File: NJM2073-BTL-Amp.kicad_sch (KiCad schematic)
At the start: 71 parts, among them J1 Screw_Terminal_01x02, J2 Screw_Terminal_01x02, U3 NJM4558, U4 NJM4558

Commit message: ラベル名変更
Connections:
- net Input renamed Input_L
- net Input_L: no longer C23.1
- new net Input_R: C23.1
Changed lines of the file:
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@@
 		)
 	)
-	(global_label "Input"
+	(global_label "Input_L"
 		(shape input)
 		(at 110.49 91.44 180)
@@
 		)
 		(property "Intersheetrefs" "${INTERSHEET_REFS}"
-			(at 102.7273 91.44 0)
+			(at 100.7316 91.44 0)
 			(effects
 				(font
@@
 		)
 	)
-	(global_label "Input"
+	(global_label "Input_R"
 		(shape input)
 		(at 110.49 180.34 180)
@@
 		)
 		(property "Intersheetrefs" "${INTERSHEET_REFS}"
-			(at 102.7273 180.34 0)
+			(at 100.4897 180.34 0)
 			(effects
 				(font

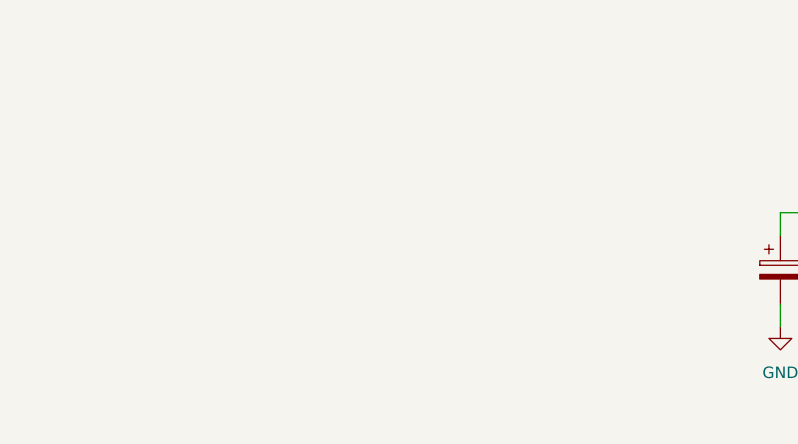
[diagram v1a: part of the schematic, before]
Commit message: 電源入力・フィルタ追加
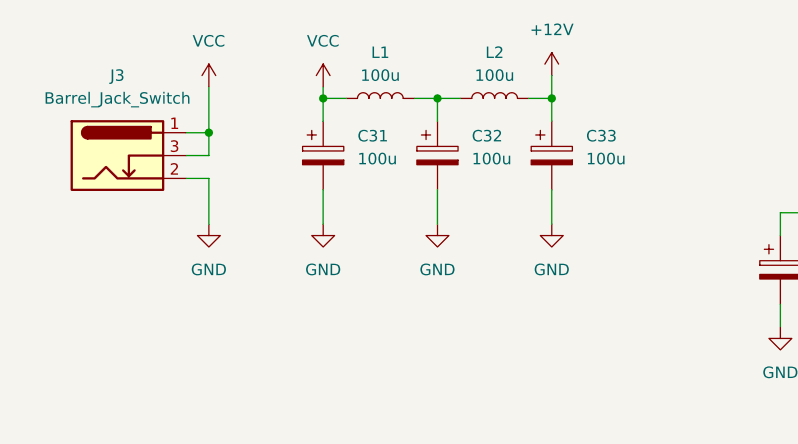
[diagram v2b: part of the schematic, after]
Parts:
- added C31, C32, C33: 100u, symbol Device:C_Polarized
- added J3: Barrel_Jack_Switch, symbol Connector:Barrel_Jack_Switch
- added L1, L2: 100u, symbol Device:L
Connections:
- net +12V: now also C33.1, L2.2
- net GND: now also C31.2, C32.2, C33.2, J3.2
- new net: C32.1, L1.2, L2.1
- new net VCC: C31.1, J3.1, J3.3, L1.1

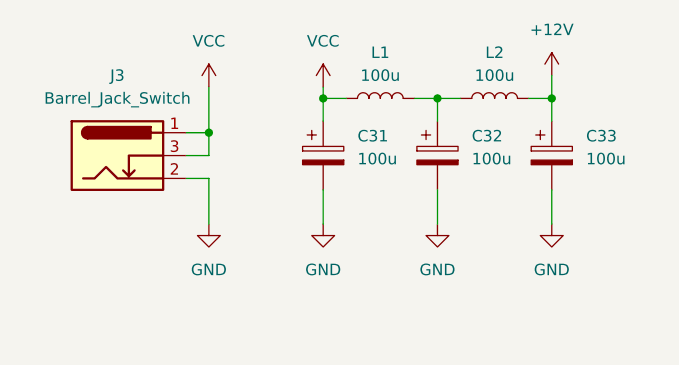
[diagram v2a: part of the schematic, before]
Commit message: 逆接保護ダイオード追加
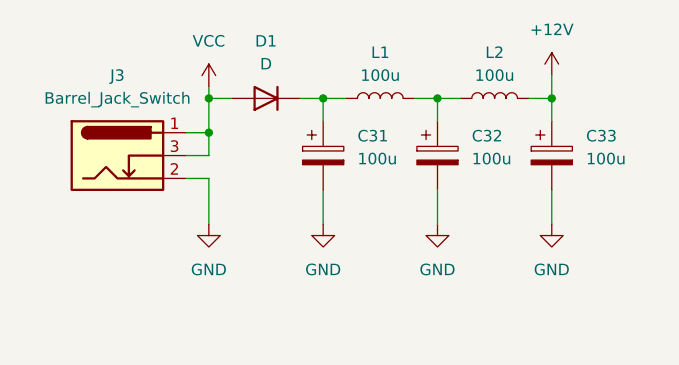
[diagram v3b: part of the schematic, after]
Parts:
- added D1: D, symbol Device:D
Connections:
- net VCC: now also D1.2 (A); no longer C31.1, L1.1
- new net: C31.1, D1.1 (K), L1.1
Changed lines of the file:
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@@
 	(paper "A3")
 	(junction
+		(at 50.8 25.4)
+		(diameter 0)
+		(color 0 0 0 0)
+	)
+	(junction
 		(at 114.3 127)
 		(diameter 0)
@@
 	)
 	(junction
+		(at 38.1 25.4)
+		(diameter 0)
+		(color 0 0 0 0)
+	)
+	(junction
 		(at 163.83 38.1)
 		(diameter 0)
@@
 	)
 	(junction
-		(at 50.8 25.4)
-		(diameter 0)
-		(color 0 0 0 0)
-	)
-	(junction
 		(at 139.7 73.66)
 		(diameter 0)
@@
 	(wire
 		(pts
+			(xy 48.26 25.4) (xy 50.8 25.4)
+		)
+		(stroke
+			(width 0)
+			(type default)
+		)
+	)
+	(wire
+		(pts
 			(xy 304.8 62.23) (xy 304.8 63.5)
 		)
@@
 	(wire
 		(pts
+			(xy 38.1 25.4) (xy 40.64 25.4)
+		)
+		(stroke
+			(width 0)
+			(type default)
+		)
+	)
+	(wire
+		(pts
 			(xy 203.2 176.53) (xy 203.2 177.8)
 		)
@@
 	(wire
 		(pts
-			(xy 38.1 24.13) (xy 38.1 29.21)
+			(xy 38.1 24.13) (xy 38.1 25.4)
 		)
 		(stroke
@@
 	(wire
 		(pts
-			(xy 50.8 24.13) (xy 50.8 25.4)
-		)
-		(stroke
-			(width 0)
-			(type default)
-		)
-	)
-	(wire
-		(pts
 			(xy 139.7 175.26) (xy 144.78 175.26)
 		)
@@
 	(wire
 		(pts
+			(xy 38.1 25.4) (xy 38.1 29.21)
+		)
+		(stroke
+			(width 0)
+			(type default)
+		)
+	)
+	(wire
+		(pts
 			(xy 163.83 125.73) (xy 163.83 127)
 		)
@@
 	)
 	(symbol
-		(lib_id "power:VCC")
-		(at 50.8 24.13 0)
-		(unit 1)
-		(exclude_from_sim no)
-		(in_bom yes)
-		(on_board yes)
-		(dnp no)
-		(fields_autoplaced yes)
-		(property "Reference" "#PWR035"
-			(at 50.8 27.94 0)
-			(effects
-				(font
-					(size 1.27 1.27)
-				)
-				(hide yes)
-			)
-		)
-		(property "Value" "VCC"
-			(at 50.8 19.05 0)
-			(effects
-				(font
-					(size 1.27 1.27)
-				)
-			)
-		)
-		(property "Footprint" ""
-			(at 50.8 24.13 0)
-			(effects
-				(font
-					(size 1.27 1.27)
-				)
-				(hide yes)
-			)
-		)
-		(property "Datasheet" ""
-			(at 50.8 24.13 0)
-			(effects
-				(font
-					(size 1.27 1.27)
-				)
-				(hide yes)
-			)
-		)
-		(property "Description" "Power symbol creates a global label with name \"VCC\""
-			(at 50.8 24.13 0)
-			(effects
-				(font
-					(size 1.27 1.27)
-				)
-				(hide yes)
-			)
-		)
-		(pin "1"
-		)
-		(instances
-			(project "NJM2073-BTL-Amp"
-				(path "/39400954-8ff9-4acb-a709-09671291994b"
-					(reference "#PWR035")
-					(unit 1)
-				)
-			)
-		)
-	)
-	(symbol
 		(lib_id "Device:R")
 		(at 335.28 165.1 90)
@@
 				)
 			)
+		)
+	)
+	(symbol
+		(lib_id "Device:D")
+		(at 44.45 25.4 180)
+		(unit 1)
+		(exclude_from_sim no)
+		(in_bom yes)
+		(on_board yes)
+		(dnp no)
+		(fields_autoplaced yes)
+		(property "Reference" "D1"
+			(at 44.45 19.05 0)
+			(effects
+				(font
+					(size 1.27 1.27)
+				)
+			)
+		)
+		(property "Value" "D"
+			(at 44.45 21.59 0)
+			(effects
+				(font
+					(size 1.27 1.27)
+				)
+			)
+		)
+		(property "Footprint" ""
+			(at 44.45 25.4 0)
+			(effects
+				(font
+					(size 1.27 1.27)
+				)
+				(hide yes)
+			)
+		)
+		(property "Datasheet" "~"
+			(at 44.45 25.4 0)
+			(effects
+				(font
+					(size 1.27 1.27)
+				)
+				(hide yes)
+			)
+		)
+		(property "Description" "Diode"
+			(at 44.45 25.4 0)
+			(effects
+				(font
+					(size 1.27 1.27)
+				)
+				(hide yes)
+			)
+		)
+		(property "Sim.Device" "D"
+			(at 44.45 25.4 0)
+			(effects
+				(font
+					(size 1.27 1.27)
+				)
+				(hide yes)
+			)
+		)
+		(property "Sim.Pins" "1=K 2=A"
+			(at 44.45 25.4 0)
+			(effects
+				(font
+					(size 1.27 1.27)
+				)
+				(hide yes)
+			)
+		)
+		(pin "2"
+		)
+		(pin "1"
+		)
+		(instances
+			(project ""
+				(path "/39400954-8ff9-4acb-a709-09671291994b"
+					(reference "D1")
+					(unit 1)
+				)
+			)

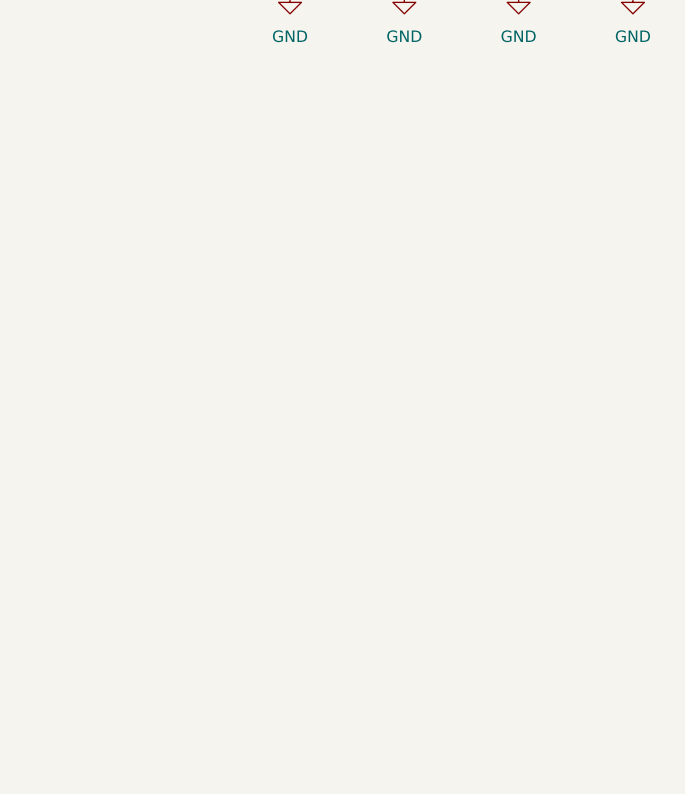
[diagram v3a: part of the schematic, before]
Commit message: 音声入力追加
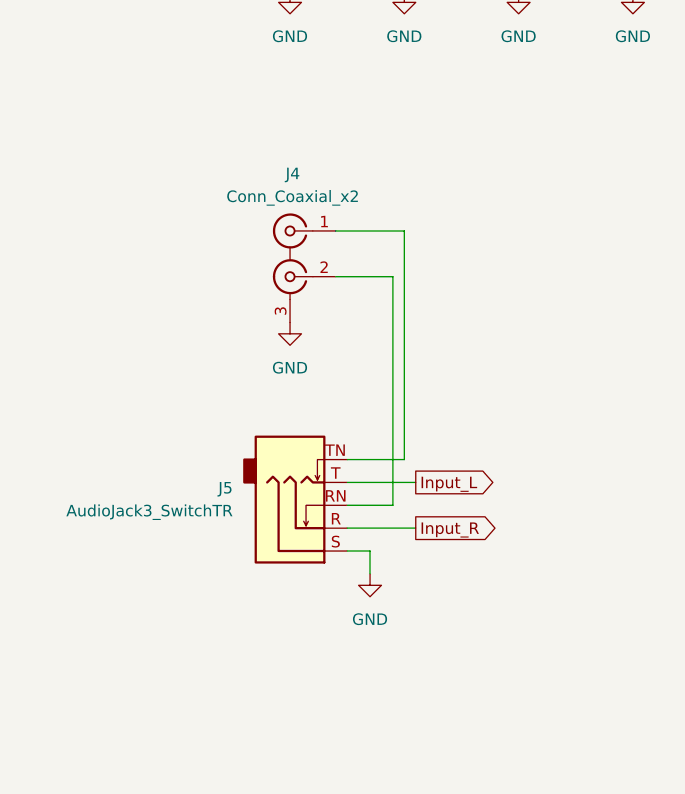
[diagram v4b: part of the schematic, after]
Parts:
- added J4: Conn_Coaxial_x2, symbol Connector:Conn_Coaxial_x2
- added J5: AudioJack3_SwitchTR, symbol Connector_Audio:AudioJack3_SwitchTR
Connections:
- net GND: now also J4.3 (EXT), J5.S
- net Input_L: now also J5.T
- net Input_R: now also J5.R
- new net: J4.2 (IN2), J5.RN
- new net: J4.1 (IN1), J5.TN

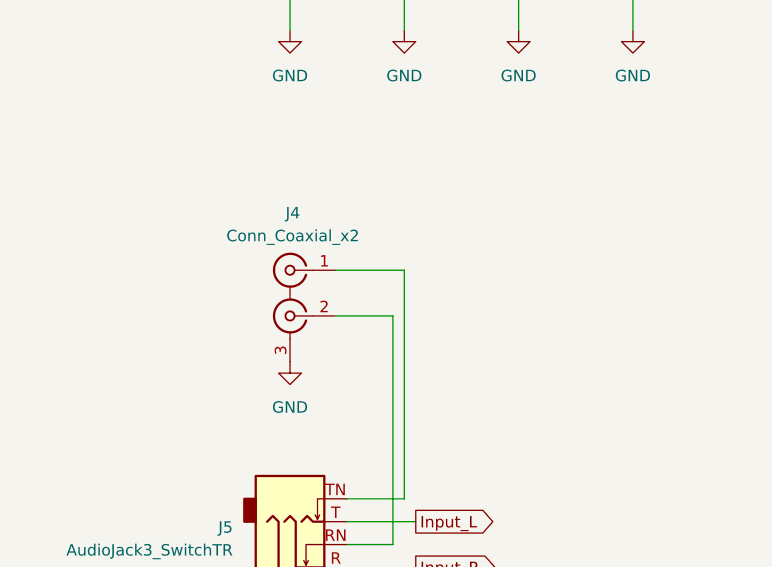
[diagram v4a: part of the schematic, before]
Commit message: フットプリント割り当て
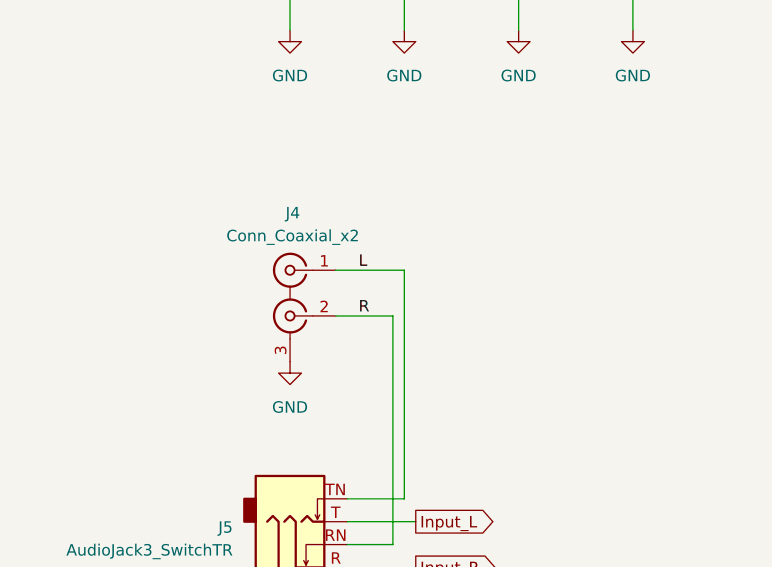
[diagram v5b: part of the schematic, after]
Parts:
- C1, C11, C12, C13, C14, C15, C16, C17, C18, C2, Copt1, Copt2: footprint (none) -> Capacitor_THT:C_Disc_D5.0mm_W2.5mm_P5.00mm
- C27, C28, C29, C30, C31, C32, C33, L1, L2: footprint (none) -> Capacitor_THT:CP_Radial_D10.0mm_P5.00mm
- D1: footprint (none) -> Diode_THT:D_A-405_P12.70mm_Horizontal
- J3: footprint (none) -> Connector_BarrelJack:BarrelJack_Horizontal
- J5: footprint (none) -> Connector_Audio:Jack_3.5mm_CUI_SJ1-3535NG_Horizontal
- RV1, RV2, RV3: footprint (none) -> Potentiometer_THT:Potentiometer_Alps_RK097_Dual_Horizontal
- Rf1, Rf2, Rf3, Rf4, Ropt1, Ropt2, Rs1, Rs2, Rs3, Rs4: footprint (none) -> Resistor_THT:R_Axial_DIN0207_L6.3mm_D2.5mm_P10.16mm_Horizontal
- U1, U2: footprint (none) -> Package_DIP:DIP-8_W7.62mm_Socket
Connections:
- net R: now reaches J4.2 (IN2), J5.RN
- net L: now reaches J4.1 (IN1), J5.TN
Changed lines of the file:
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@@
 		)
 	)
+	(label "R"
+		(at 45.72 71.12 0)
+		(fields_autoplaced yes)
+		(effects
+			(font
+				(size 1.27 1.27)
+			)
+			(justify left bottom)
+		)
+	)
+	(label "L"
+		(at 45.72 66.04 0)
+		(fields_autoplaced yes)
+		(effects
+			(font
+				(size 1.27 1.27)
+			)
+			(justify left bottom)
+		)
+	)
 	(global_label "Input_R"
 		(shape output)
@@
 			)
 		)
-		(property "Footprint" ""
+		(property "Footprint" "Potentiometer_THT:Potentiometer_Alps_RK097_Dual_Horizontal"
 			(at 203.2 50.8 0)
 			(effects
@@
 			)
 		)
-		(property "Footprint" ""
+		(property "Footprint" "Connector_Audio:Jack_3.5mm_CUI_SJ1-3535NG_Horizontal"
 			(at 39.37 99.06 0)
 			(effects
@@
 			)
 		)
-		(property "Footprint" ""
+		(property "Footprint" "Resistor_THT:R_Axial_DIN0207_L6.3mm_D2.5mm_P10.16mm_Horizontal"
 			(at 366.522 63.5 90)
 			(effects
@@
 			)
 		)
-		(property "Footprint" ""
+		(property "Footprint" "Package_DIP:DIP-8_W7.62mm_Socket"
 			(at 342.9 145.288 0)
 			(effects
@@
 			)
 		)
-		(property "Footprint" ""
+		(property "Footprint" "Capacitor_THT:C_Disc_D5.0mm_W2.5mm_P5.00mm"
 			(at 305.7652 151.13 0)
 			(effects
@@
 			)
 		)
-		(property "Footprint" ""
+		(property "Footprint" "Capacitor_THT:C_Disc_D5.0mm_W2.5mm_P5.00mm"
 			(at 324.8152 173.99 0)
 			(effects
@@
 			)
 		)
-		(property "Footprint" ""
+		(property "Footprint" "Capacitor_THT:C_Disc_D5.0mm_W2.5mm_P5.00mm"
 			(at 305.7652 99.06 0)
 			(effects
@@
 			)
 		)
-		(property "Footprint" ""
+		(property "Footprint" "Capacitor_THT:CP_Radial_D10.0mm_P5.00mm"
 			(at 102.5652 137.16 0)
 			(effects
@@
 			)
 		)
-		(property "Footprint" ""
+		(property "Footprint" "Resistor_THT:R_Axial_DIN0207_L6.3mm_D2.5mm_P10.16mm_Horizontal"
 			(at 317.5 65.278 90)
 			(effects
@@
 			)
 		)
-		(property "Footprint" ""
+		(property "Footprint" "Capacitor_THT:CP_Radial_D10.0mm_P5.00mm"
 			(at 64.4652 35.56 0)
 			(effects
@@
 			)
 		)
-		(property "Footprint" ""
+		(property "Footprint" "Resistor_THT:R_Axial_DIN0207_L6.3mm_D2.5mm_P10.16mm_Horizontal"
 			(at 317.5 154.178 90)
 			(effects
@@
 			)
 		)
-		(property "Footprint" ""
+		(property "Footprint" "Capacitor_THT:CP_Radial_D10.0mm_P5.00mm"
 			(at 77.1652 35.56 0)
 			(effects
@@
 			)
 		)
-		(property "Footprint" ""
+		(property "Footprint" "Resistor_THT:R_Axial_DIN0207_L6.3mm_D2.5mm_P10.16mm_Horizontal"
 			(at 335.28 65.278 90)
 			(effects
@@
 			)
 		)
-		(property "Footprint" ""
+		(property "Footprint" "Capacitor_THT:C_Disc_D5.0mm_W2.5mm_P5.00mm"
 			(at 305.7652 62.23 0)
 			(effects
@@
 			)
 		)
-		(property "Footprint" ""
+		(property "Footprint" "Resistor_THT:R_Axial_DIN0207_L6.3mm_D2.5mm_P10.16mm_Horizontal"
 			(at 317.5 77.978 90)
 			(effects
@@
 			)
 		)
-		(property "Footprint" ""
+		(property "Footprint" "Capacitor_THT:C_Disc_D5.0mm_W2.5mm_P5.00mm"
 			(at 356.5652 130.81 0)
 			(effects
@@
 			)
 		)
-		(property "Footprint" ""
+		(property "Footprint" "Package_DIP:DIP-8_W7.62mm_Socket"
 			(at 342.9 56.388 0)
 			(effects
@@
 			)
 		)
-		(property "Footprint" ""
+		(property "Footprint" "Resistor_THT:R_Axial_DIN0207_L6.3mm_D2.5mm_P10.16mm_Horizontal"
 			(at 335.28 77.978 90)
 			(effects
@@
 			)
 		)
-		(property "Footprint" ""
+		(property "Footprint" "Capacitor_THT:C_Disc_D5.0mm_W2.5mm_P5.00mm"
 			(at 324.8152 151.13 0)
 			(effects
@@
 			)
 		)
-		(property "Footprint" ""
+		(property "Footprint" "Capacitor_THT:C_Disc_D5.0mm_W2.5mm_P5.00mm"
 			(at 324.8152 85.09 0)
 			(effects
@@
 			)
 		)
-		(property "Footprint" ""
+		(property "Footprint" "Capacitor_THT:C_Disc_D5.0mm_W2.5mm_P5.00mm"
 			(at 369.2652 80.01 0)
 			(effects
@@
 			)
 		)
-		(property "Footprint" ""
+		(property "Footprint" "Potentiometer_THT:Potentiometer_Alps_RK097_Dual_Horizontal"
 			(at 292.1 137.16 0)
 			(effects
@@
 			)
 		)
-		(property "Footprint" ""
+		(property "Footprint" "Capacitor_THT:CP_Radial_D10.0mm_P5.00mm"
 			(at 369.2652 41.91 0)
 			(effects
@@
 			)
 		)
-		(property "Footprint" ""
+		(property "Footprint" "Resistor_THT:R_Axial_DIN0207_L6.3mm_D2.5mm_P10.16mm_Horizontal"
 			(at 366.522 152.4 90)
 			(effects
@@
 			)
 		)
-		(property "Footprint" ""
+		(property "Footprint" "Connector_BarrelJack:BarrelJack_Horizontal"
 			(at 29.21 32.766 0)
 			(effects
@@
 			)
 		)
-		(property "Footprint" ""
+		(property "Footprint" "Capacitor_THT:CP_Radial_D10.0mm_P5.00mm"
 			(at 369.2652 130.81 0)
 			(effects
@@
 			)
 		)
-		(property "Footprint" ""
+		(property "Footprint" "Resistor_THT:R_Axial_DIN0207_L6.3mm_D2.5mm_P10.16mm_Horizontal"
 			(at 317.5 166.878 90)
 			(effects
@@
 			)
 		)
-		(property "Footprint" ""
+		(property "Footprint" "Package_DIP:DIP-8_W7.62mm_Socket"
 			(at 342.9 183.388 0)
 			(effects
@@
 			)
 		)
-		(property "Footprint" ""
+		(property "Footprint" "Capacitor_THT:C_Disc_D5.0mm_W2.5mm_P5.00mm"
 			(at 356.5652 41.91 0)
 			(effects
@@
 			)
 		)
-		(property "Footprint" ""
+		(property "Footprint" "Resistor_THT:R_Axial_DIN0207_L6.3mm_D2.5mm_P10.16mm_Horizontal"
 			(at 335.28 154.178 90)
 			(effects
@@
 			)
 		)
-		(property "Footprint" ""
+		(property "Footprint" "Resistor_THT:R_Axial_DIN0207_L6.3mm_D2.5mm_P10.16mm_Horizontal"
 			(at 335.28 166.878 90)
 			(effects
@@
 			)
 		)
-		(property "Footprint" ""
+		(property "Footprint" "Potentiometer_THT:Potentiometer_Alps_RK097_Dual_Horizontal"
 			(at 203.2 139.7 0)
 			(effects
@@
 			)
 		)
-		(property "Footprint" ""
+		(property "Footprint" "Capacitor_THT:C_Disc_D5.0mm_W2.5mm_P5.00mm"
 			(at 369.2652 168.91 0)
 			(effects
@@
 			)
 		)
-		(property "Footprint" ""
+		(property "Footprint" "Potentiometer_THT:Potentiometer_Alps_RK097_Dual_Horizontal"
 			(at 203.2 101.6 0)
 			(effects
@@
 			)
 		)
-		(property "Footprint" ""
+		(property "Footprint" "Capacitor_THT:C_Disc_D5.0mm_W2.5mm_P5.00mm"
 			(at 324.8152 62.23 0)
 			(effects
@@
 			)
 		)
-		(property "Footprint" ""
+		(property "Footprint" "Package_DIP:DIP-8_W7.62mm_Socket"
 			(at 342.9 94.488 0)
 			(effects
@@
 			)
 		)
-		(property "Footprint" ""
+		(property "Footprint" "Potentiometer_THT:Potentiometer_Alps_RK097_Dual_Horizontal"
 			(at 292.1 48.26 0)
 			(effects
@@
 			)
 		)
-		(property "Footprint" ""
+		(property "Footprint" "Capacitor_THT:CP_Radial_D10.0mm_P5.00mm"
 			(at 57.15 25.4 0)
 			(effects
@@
 			)
 		)
-		(property "Footprint" ""
+		(property "Footprint" "Capacitor_THT:CP_Radial_D10.0mm_P5.00mm"
 			(at 69.85 25.4 0)
 			(effects
@@
 			)
 		)
-		(property "Footprint" ""
+		(property "Footprint" "Diode_THT:D_A-405_P12.70mm_Horizontal"
 			(at 44.45 25.4 0)
 			(effects
@@
 			)
 		)
-		(property "Footprint" ""
+		(property "Footprint" "Capacitor_THT:CP_Radial_D10.0mm_P5.00mm"
 			(at 51.7652 35.56 0)
 			(effects
@@
 			)
 		)
-		(property "Footprint" ""
+		(property "Footprint" "Capacitor_THT:CP_Radial_D10.0mm_P5.00mm"
 			(at 102.5652 48.26 0)
 			(effects
@@
 			)
 		)
-		(property "Footprint" ""
+		(property "Footprint" "Capacitor_THT:C_Disc_D5.0mm_W2.5mm_P5.00mm"
 			(at 305.7652 187.96 0)
 			(effects
@@
 			)
 		)
-		(property "Footprint" ""
+		(property "Footprint" "Potentiometer_THT:Potentiometer_Alps_RK097_Dual_Horizontal"
 			(at 203.2 190.5 0)
 			(effects

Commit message: フットプリント修正
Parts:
- J4: footprint (none) -> my:MJ-519
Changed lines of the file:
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@@
 			)
 		)
-		(property "Footprint" ""
+		(property "Footprint" "my:MJ-519"
 			(at 38.1 71.12 0)
 			(effects
